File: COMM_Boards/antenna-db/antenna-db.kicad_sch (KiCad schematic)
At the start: 49 parts, among them J1 Conn_01x03, J2 Conn_01x04, J3 Conn_01x02_Male, J6 Conn_01x02_Male, SW1 SW_SPST, SW2 SW_SPST, SW3 SW_SPST, SW4 SW_SPST, T1 MABA-007159-000000, T2 MABA-007159-000000, U1 SC4216HSETRT, U2 STM32F030CCT6, U3 SC4216HSETRT, U4 74AHC1G08, U5 74AHC1G08

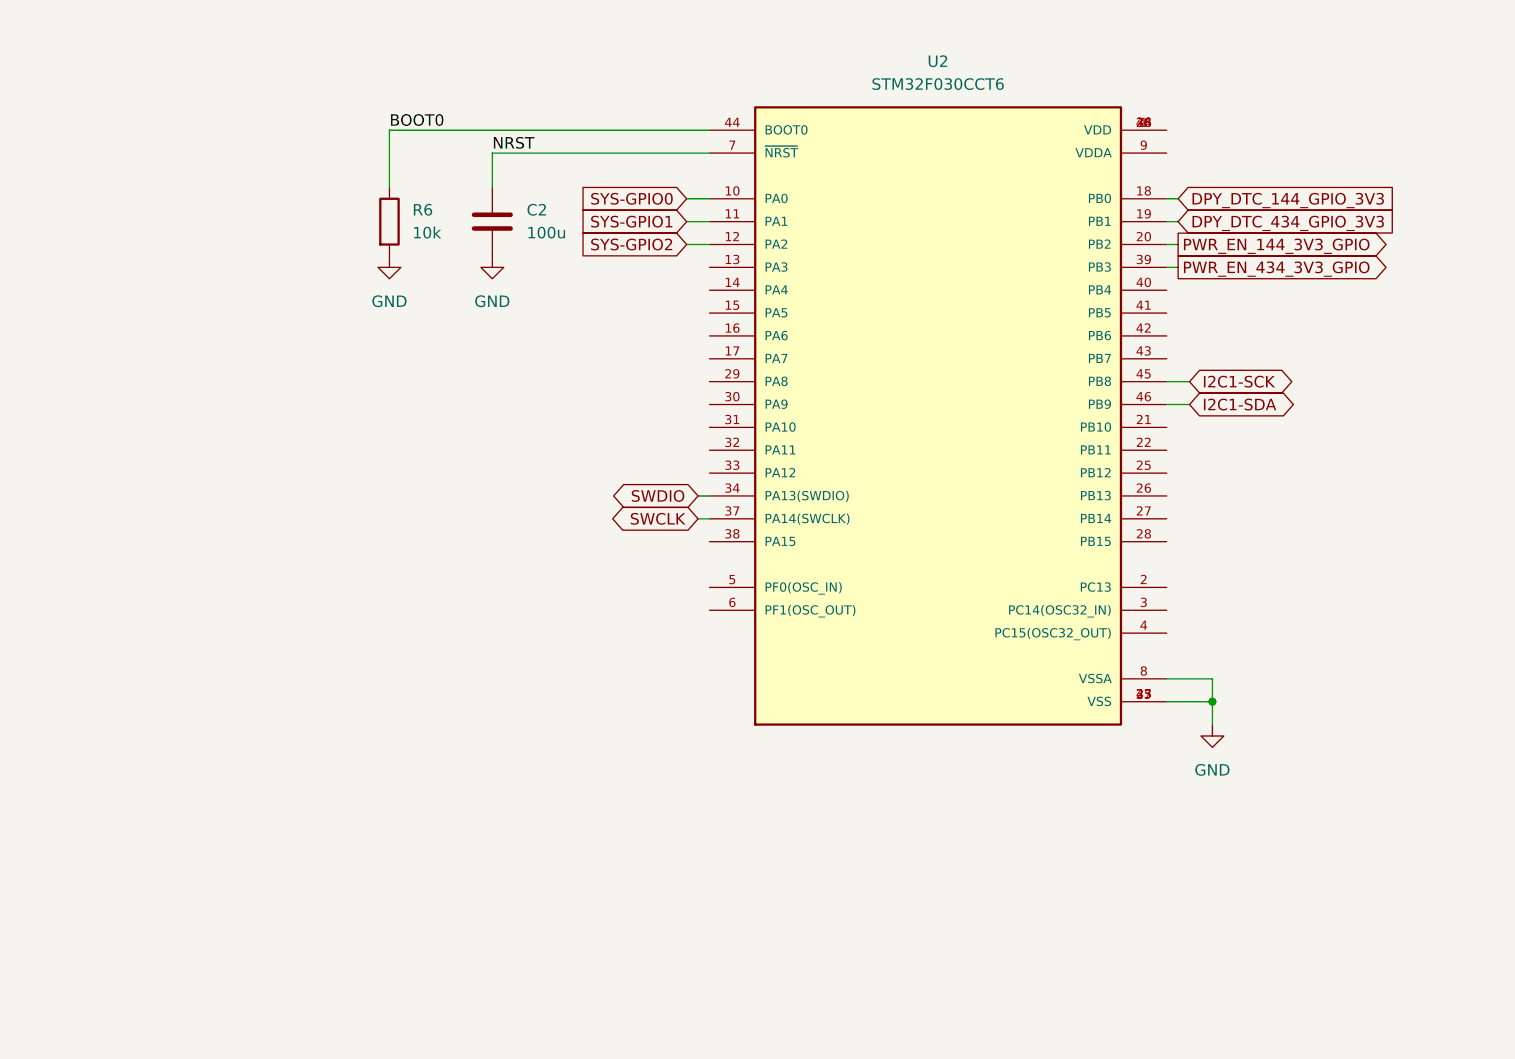
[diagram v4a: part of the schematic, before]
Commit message: COMM: antt-dbd: begin layout
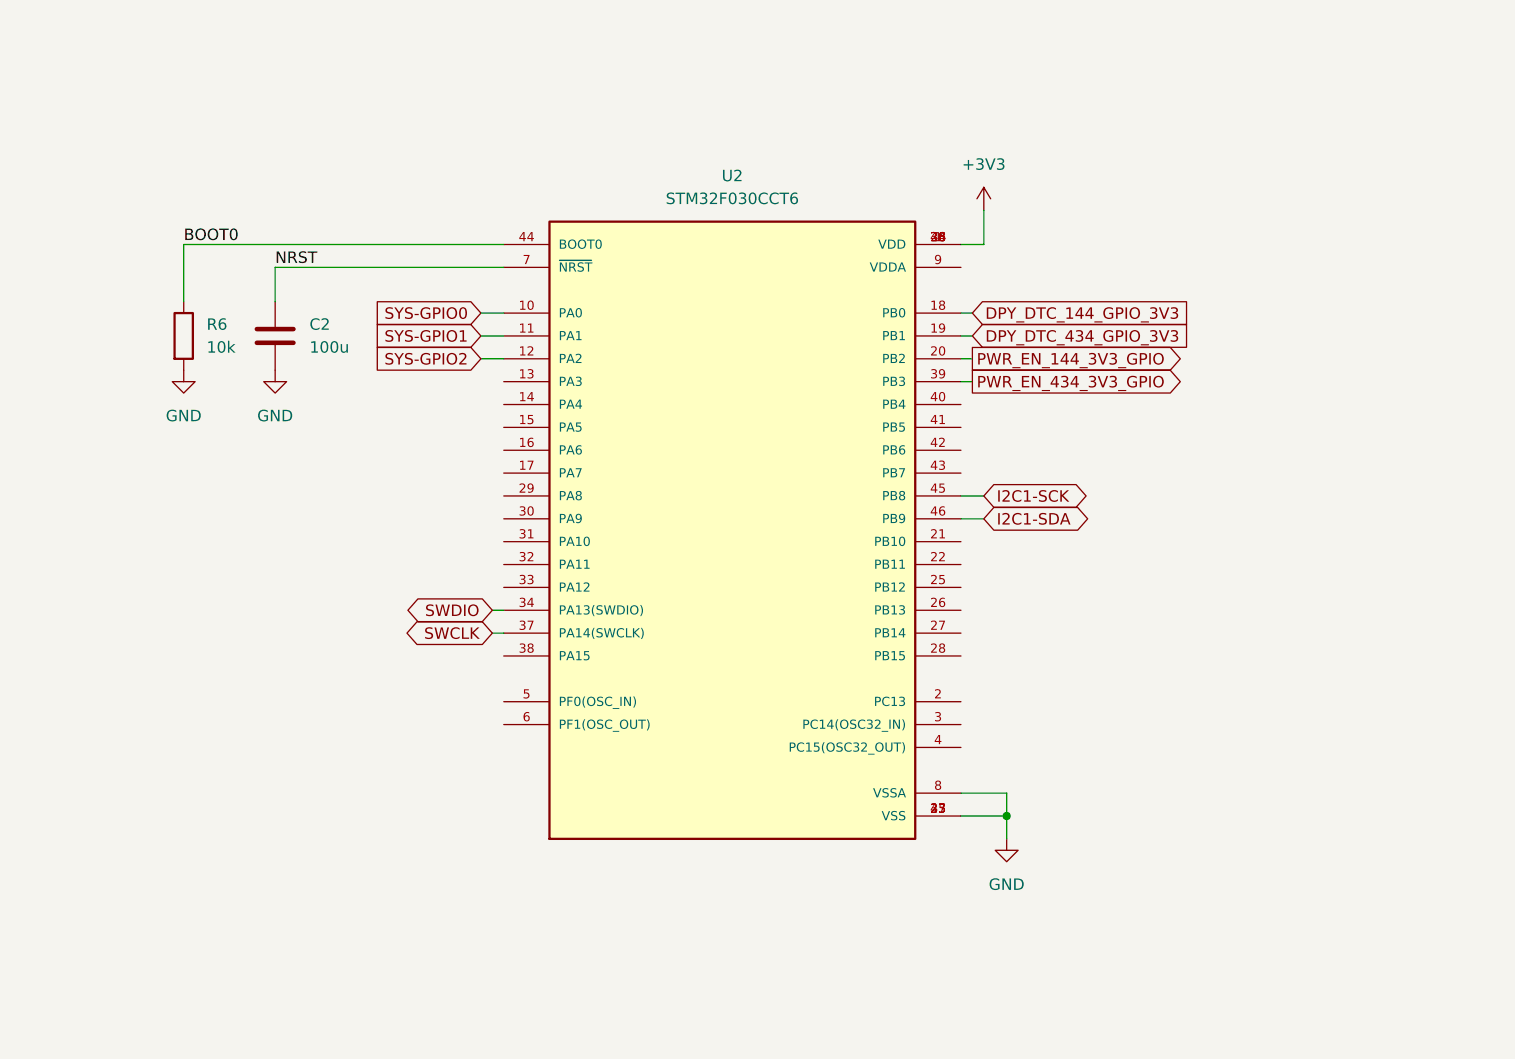
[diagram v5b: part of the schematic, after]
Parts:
- TP1, TP2: footprint TestPoint:TestPoint_THTPad_4.0x4.0mm_Drill2.0mm -> TestPoint:TestPoint_Plated_Hole_D2.0mm
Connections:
- net +3V3: now also U2.1 (VDD), U2.24 (VDD), U2.36 (VDD), U2.48 (VDD)
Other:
- moved on the sheet: C2, R6, U2

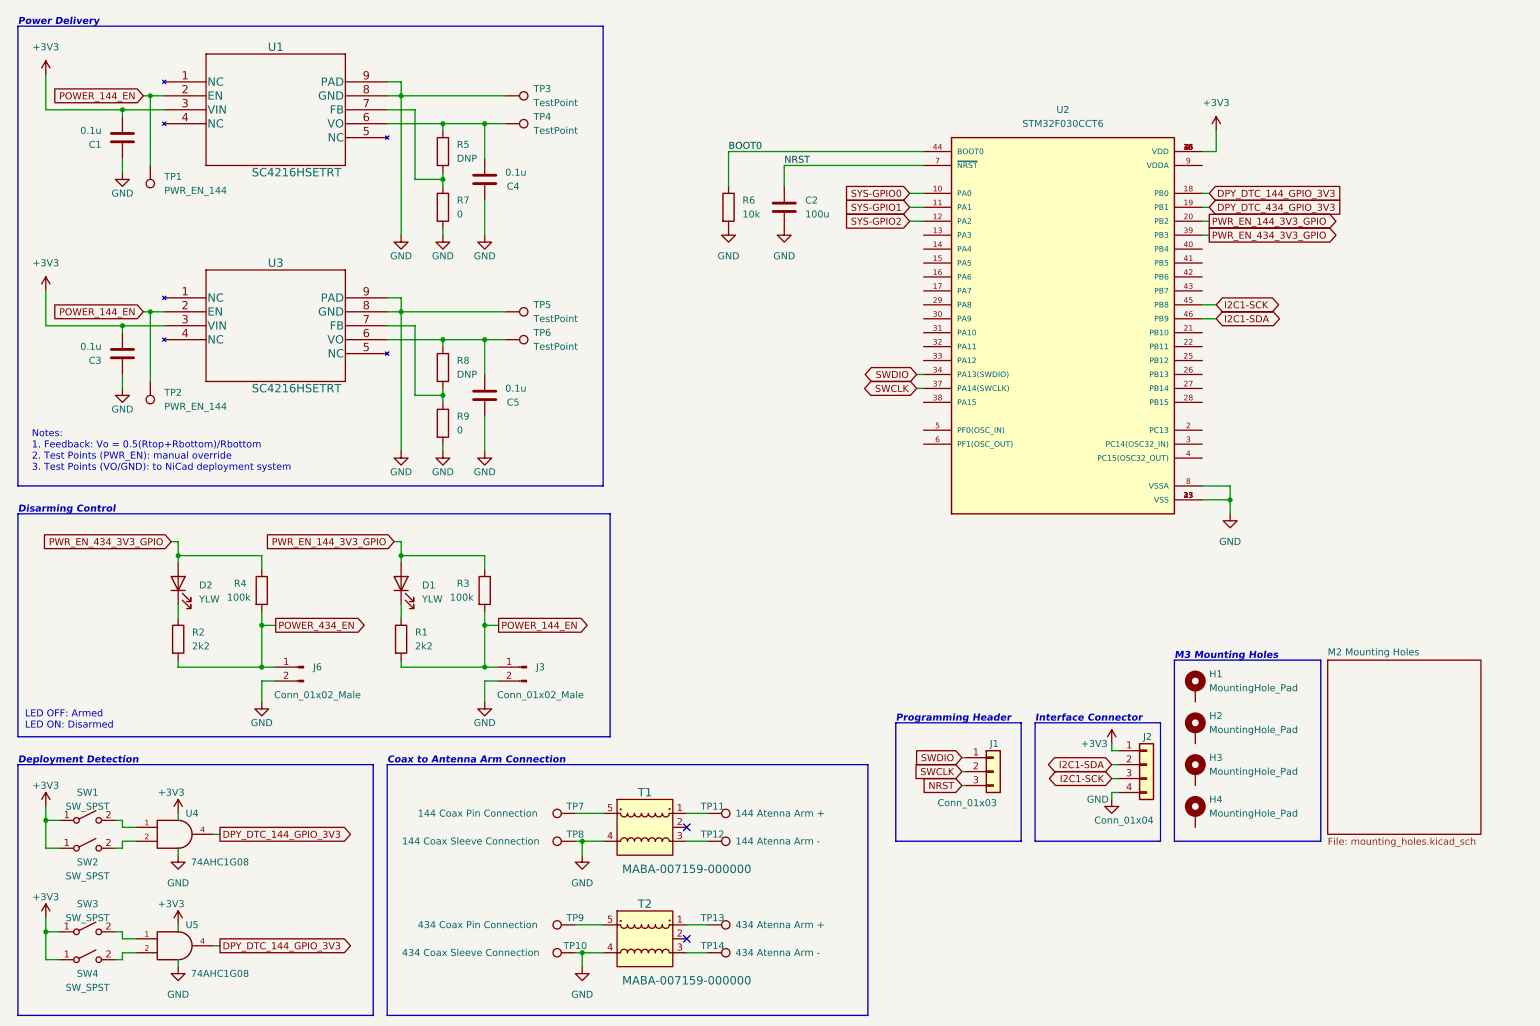
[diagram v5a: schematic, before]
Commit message: finish layout of ANTT-DBD
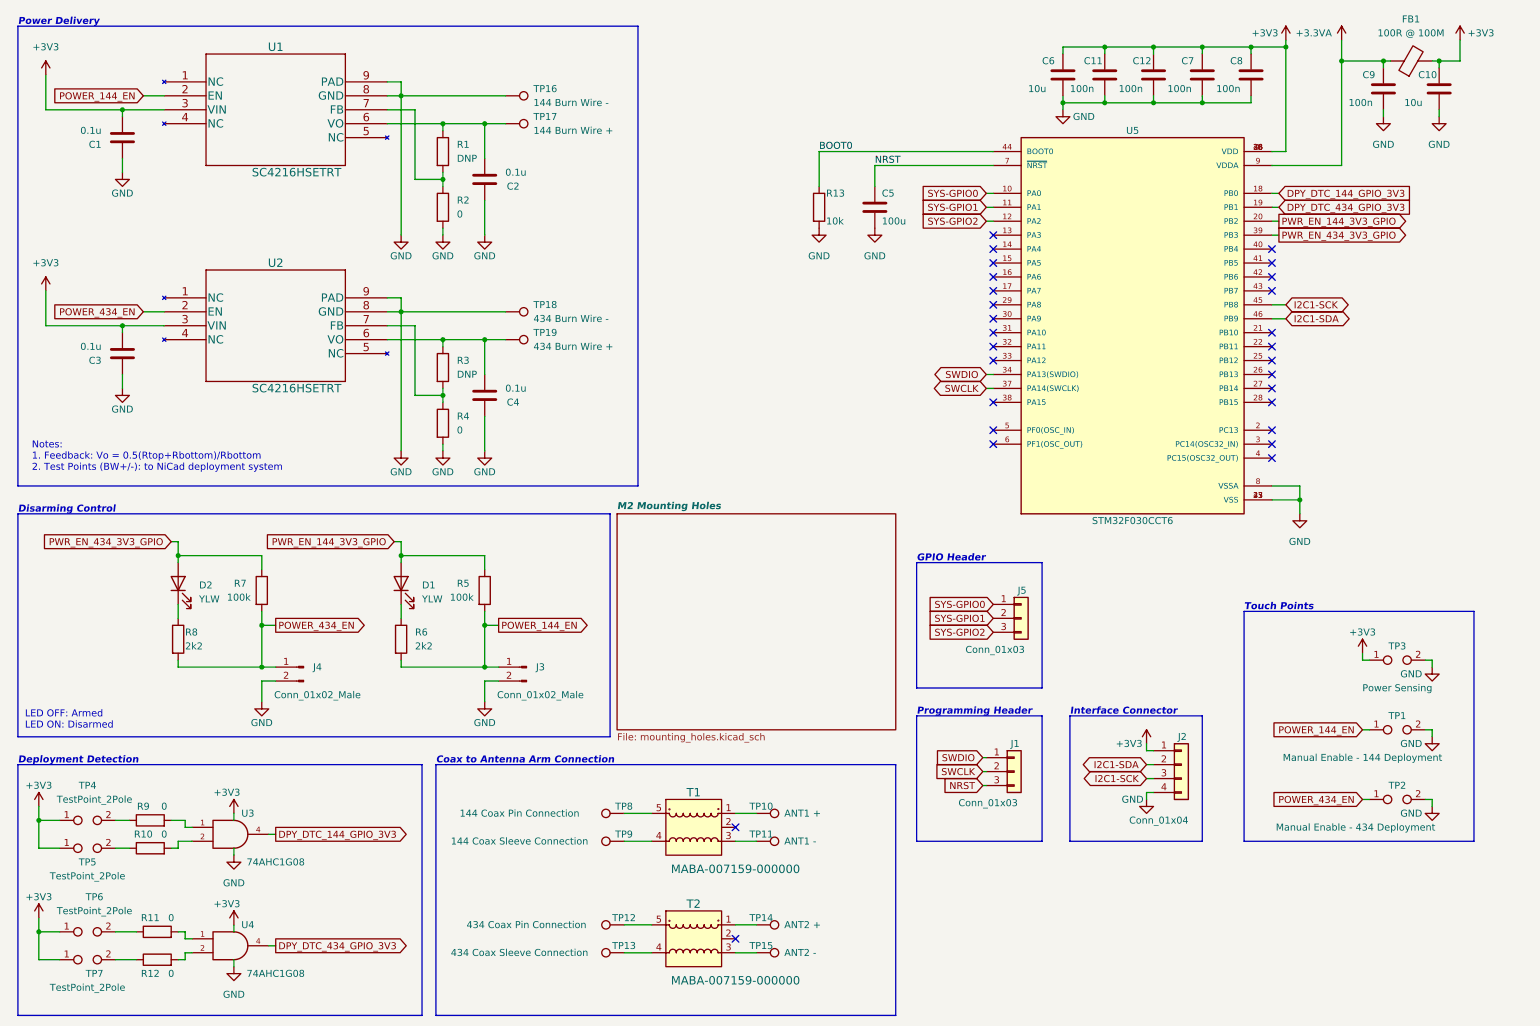
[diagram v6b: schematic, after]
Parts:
- removed H1, H2, H3, H4: MountingHole_Pad, MountingHole:MountingHole_3.2mm_M3_Pad_TopBottom, symbol Mechanical:MountingHole_Pad
- removed SW1, SW2, SW3, SW4: SW_SPST, symbol Switch:SW_SPST
- removed TP1, TP2: PWR_EN_144, TestPoint:TestPoint_Plated_Hole_D2.0mm, symbol Connector:TestPoint
- added C10, C6: 10u, Capacitor_SMD:C_0603_1608Metric, symbol Device:C
- added C11, C12, C7, C8, C9: 100n, Capacitor_SMD:C_0603_1608Metric, symbol Device:C
- added FB1: 100R @ 100M, Inductor_SMD:L_0603_1608Metric, symbol Device:FerriteBead
- added J5: Conn_01x03, qset-footprints:SAMTEC_TSM-103-01-L-SH, symbol Connector_Generic:Conn_01x03
- added R10, R11, R12, R9: 0, Resistor_SMD:R_0603_1608Metric, symbol Device:R
- added TP1: Manual Enable - 144 Deployment, TestPoint:TestPoint_2Pads_Pitch2.54mm_Drill0.8mm, symbol Connector:TestPoint_2Pole
- added TP2: Manual Enable - 434 Deployment, TestPoint:TestPoint_2Pads_Pitch2.54mm_Drill0.8mm, symbol Connector:TestPoint_2Pole
- added TP3: Power Sensing, TestPoint:TestPoint_2Pads_Pitch2.54mm_Drill0.8mm, symbol Connector:TestPoint_2Pole
- added TP4, TP5, TP6, TP7: TestPoint_2Pole, TestPoint:TestPoint_2Pads_Pitch2.54mm_Drill0.8mm, symbol Connector:TestPoint_2Pole
- J1: footprint Connector_PinHeader_2.54mm:PinHeader_1x03_P2.54mm_Horizontal -> qset-footprints:SAMTEC_TSM-103-01-L-SH
- J2: footprint Connector_PinHeader_2.54mm:PinHeader_1x04_P2.54mm_Horizontal -> qset-footprints:SAMTEC_TSM-104-01-L-SH
- J3: footprint Connector_PinHeader_2.54mm:PinHeader_1x02_P2.54mm_Horizontal -> qset-footprints:SAMTEC_TSM-102-01-L-SH
- J4: renamed from J6; footprint Connector_PinHeader_2.54mm:PinHeader_1x02_P2.54mm_Horizontal -> qset-footprints:SAMTEC_TSM-102-01-L-SH
- TP10: renamed from TP11; value 144 Atenna Arm + -> ANT1 +
- TP11: renamed from TP12; value 144 Atenna Arm - -> ANT1 -
- TP12: renamed from TP9; footprint TestPoint:TestPoint_THTPad_4.0x4.0mm_Drill2.0mm -> TestPoint:TestPoint_THTPad_2.0x2.0mm_Drill1.0mm
- TP13: renamed from TP10; footprint TestPoint:TestPoint_THTPad_4.0x4.0mm_Drill2.0mm -> TestPoint:TestPoint_THTPad_2.0x2.0mm_Drill1.0mm
- TP14: renamed from TP13; value 434 Atenna Arm + -> ANT2 +
- TP15: renamed from TP14; value 434 Atenna Arm - -> ANT2 -
- TP16: renamed from TP3; value TestPoint -> 144 Burn Wire -; footprint TestPoint:TestPoint_THTPad_4.0x4.0mm_Drill2.0mm -> TestPoint:TestPoint_THTPad_2.0x2.0mm_Drill1.0mm
- TP17: renamed from TP4; value TestPoint -> 144 Burn Wire +; footprint TestPoint:TestPoint_THTPad_4.0x4.0mm_Drill2.0mm -> TestPoint:TestPoint_THTPad_2.0x2.0mm_Drill1.0mm
- TP18: renamed from TP5; value TestPoint -> 434 Burn Wire -; footprint TestPoint:TestPoint_THTPad_4.0x4.0mm_Drill2.0mm -> TestPoint:TestPoint_THTPad_2.0x2.0mm_Drill1.0mm
- TP19: renamed from TP6; value TestPoint -> 434 Burn Wire +; footprint TestPoint:TestPoint_THTPad_4.0x4.0mm_Drill2.0mm -> TestPoint:TestPoint_THTPad_2.0x2.0mm_Drill1.0mm
- TP8: renamed from TP7; footprint TestPoint:TestPoint_THTPad_4.0x4.0mm_Drill2.0mm -> TestPoint:TestPoint_THTPad_2.0x2.0mm_Drill1.0mm
- TP9: renamed from TP8; footprint TestPoint:TestPoint_THTPad_4.0x4.0mm_Drill2.0mm -> TestPoint:TestPoint_THTPad_2.0x2.0mm_Drill1.0mm
- renumbered C4 to C2, C5 to C4, C2 to C5, R5 to R1, R6 to R13, R7 to R2, R8 to R3, R9 to R4, R3 to R5, R1 to R6, R4 to R7, R2 to R8, U3 to U2, U4 to U3, U5 to U4, U2 to U5
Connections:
- net +3V3: now also C10.1, C11.1, C12.1, C6.1, C7.1, C8.1, FB1.2, TP3.1, TP4.1, TP5.1, TP6.1, TP7.1
- net DPY_DTC_144_GPIO_3V3: no longer U4.4
- net DPY_DTC_434_GPIO_3V3: now also U4.4
- net GND: now also C10.2, C11.2, C12.2, C6.2, C7.2, C8.2, C9.2, TP1.2, TP2.2, TP3.2; no longer T1.4, T2.4, TP13.1, TP9.1
- net POWER_144_EN: now also TP1.1; no longer U2.2 (EN)
- net POWER_434_EN: now also U2.2 (EN), TP2.1
- net SYS-GPIO0: now also J5.1 (Pin_1)
- net SYS-GPIO1: now also J5.2 (Pin_2)
- net SYS-GPIO2: now also J5.3 (Pin_3)
- net at U4.1: now also R11.2
- net at U3.1: now also R9.2
- net at U3.2: now also R10.2
- net +3.3VA: now reaches U5.9 (VDDA)
- net +3.3VA: now also C9.1, FB1.1
- net at U4.2: now also R12.2
- new net: R12.1, TP7.2
- new net: R9.1, TP4.2
- new net: T1.4, TP9.1
- new net: T2.4, TP13.1
- new net: R11.1, TP6.2
- new net: R10.1, TP5.2
- no-connect marks 2 -> 28
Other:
- note added: "GPIO Header"
- note added: "Notes: 1. Feedback: Vo = 0.5(Rtop+Rbottom)/Rbottom 2. Test Points (BW+/-): to NiCad deployment system"
- note added: "Touch Points"
- note removed: "M3 Mounting Holes"
- note removed: "Notes: 1. Feedback: Vo = 0.5(Rtop+Rbottom)/Rbottom 2. Test Points (PWR_EN): manual override 3. Test Points (VO/GND): to NiCad deployment system"
- moved on the sheet: C5, J1, J2, R13, T1, T2, TP10, TP11, TP12, TP13, TP14, TP15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

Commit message: COMM: include manufacturing and assembly files
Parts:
- C5: value 100u -> 10u
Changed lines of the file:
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@@
       (effects (font (size 1.27 1.27)) (justify left))
     )
-    (property "Value" "100u" (id 1) (at 172.72 50.8 0)
+    (property "Value" "10u" (id 1) (at 172.72 50.8 0)
       (effects (font (size 1.27 1.27)) (justify left))
     )
@@
     )
     (path "/fba956d2-0475-4ba3-85dc-be0811c248e5"
-      (reference "C5") (unit 1) (value "100u") (footprint "Capacitor_SMD:C_0603_1608Metric")
+      (reference "C5") (unit 1) (value "10u") (footprint "Capacitor_SMD:C_0603_1608Metric")
     )
     (path "/f0bf3279-c9b9-4254-a927-5cf0786a4656"
